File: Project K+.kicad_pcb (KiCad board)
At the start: 2 copper layers, 76.2 x 133.4 mm, 155 parts, among them J1 USB_C_Receptacle_USB2.0, J2 USB Breakout, J3 Conn_01x03_Male, SW1 Rotary_Encoder_Switch, SW2 Rotary_Encoder_Switch, SW3 Rotary_Encoder_Switch, SW4 Rotary_Encoder_Switch, U1 ProMicro, U10 WS2811, U11 WS2811, U12 WS2811, U13 WS2811, U14 WS2811, U15 WS2811, U16 WS2811, U17 WS2811, U18 WS2811, U19 WS2811, U2 WS2811, U20 WS2811, U21 WS2811, U3 WS2811, U4 WS2811, U5 WS2811, U6 WS2811, U7 WS2811, U8 WS2811, U9 WS2811

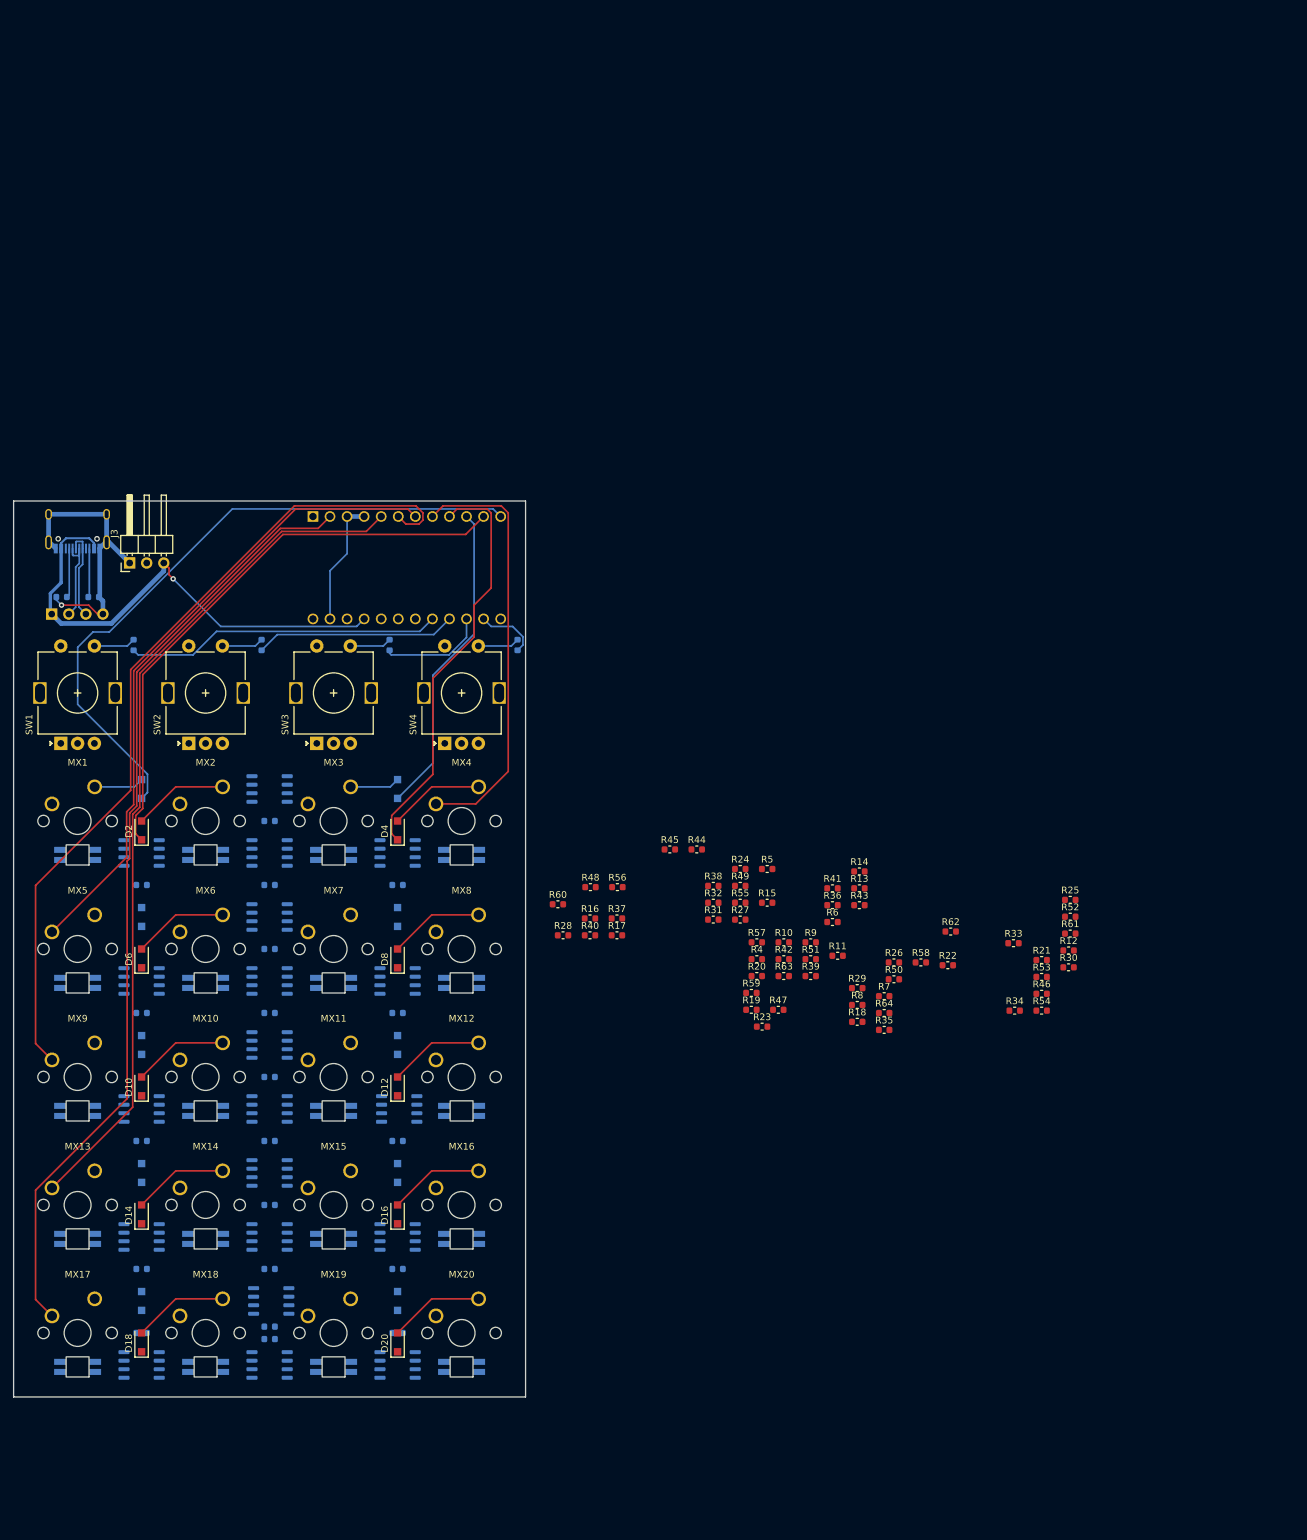
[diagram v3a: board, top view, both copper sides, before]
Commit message: Add 3D keyboard layout
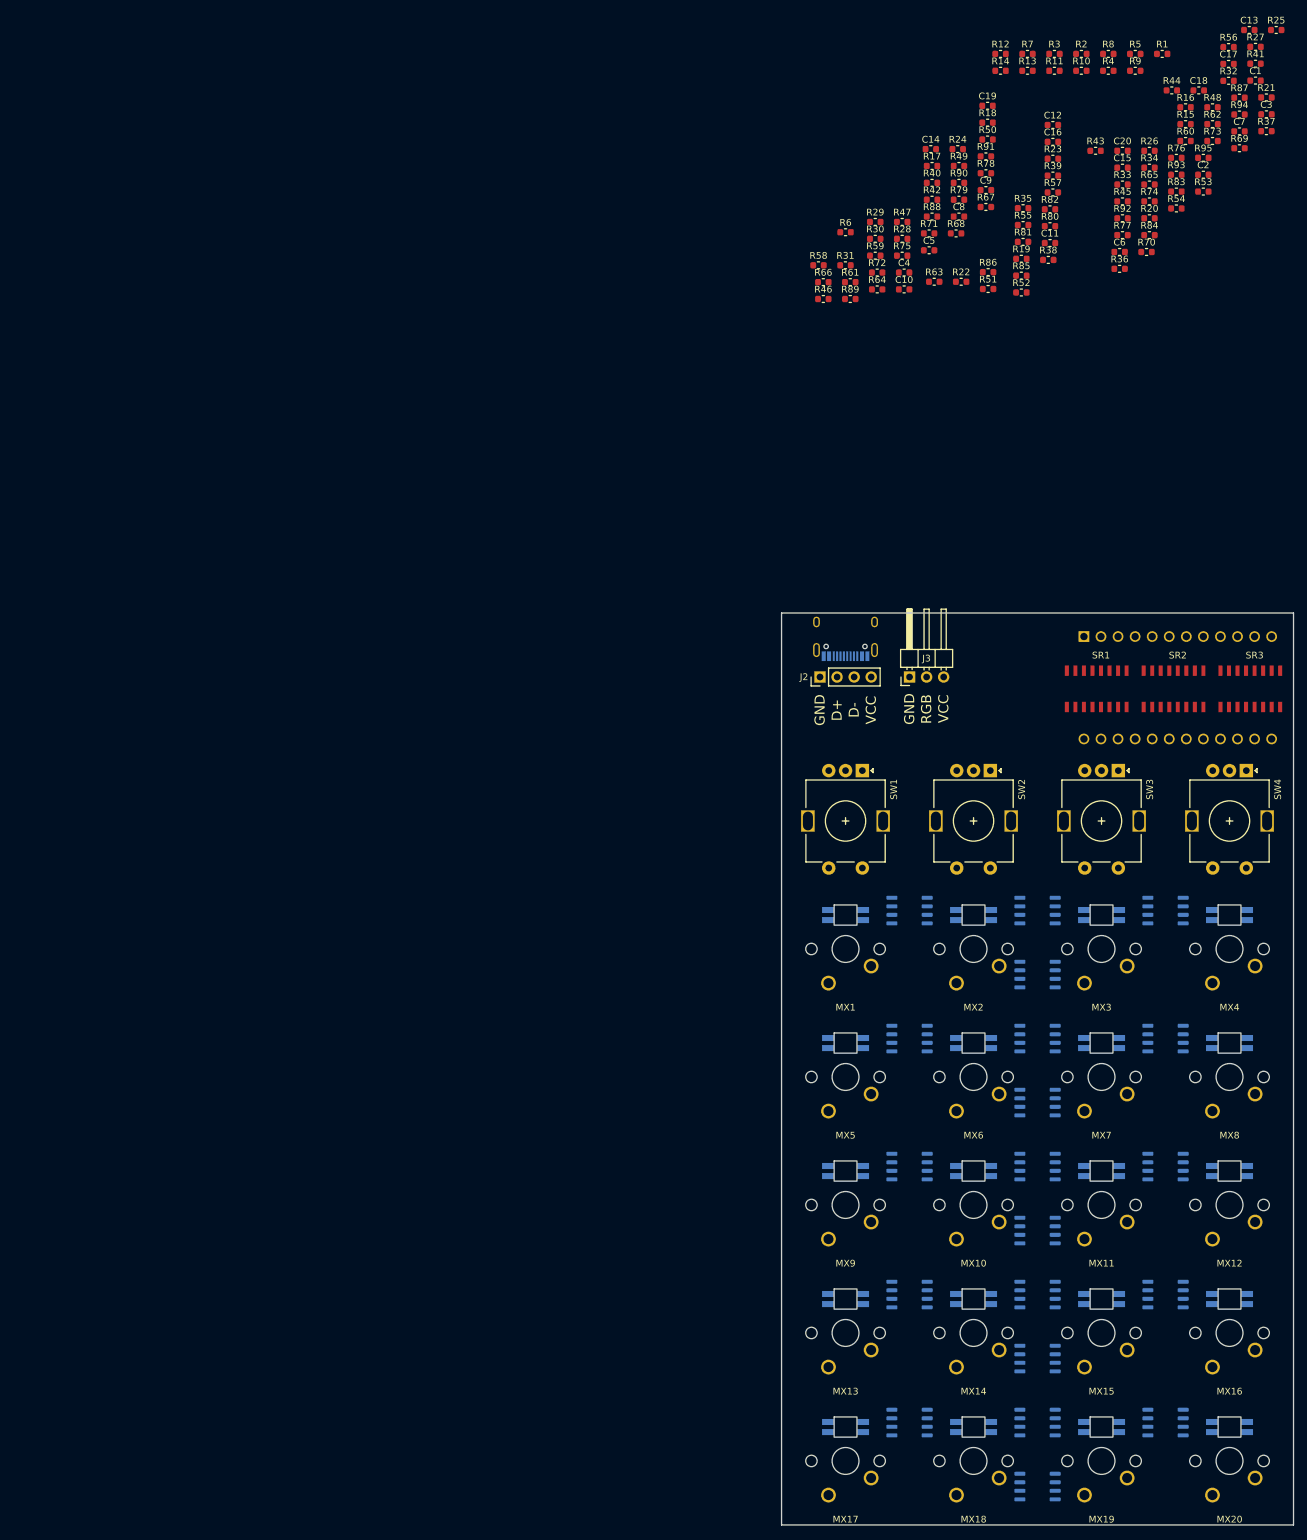
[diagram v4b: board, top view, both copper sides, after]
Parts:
- removed D1, D10, D11, D12, D13, D14, D15, D16, D17, D18, D19, D2, D20, D3, D4, D5, D6, D7, D8, D9: D_ALT, Diode_SMD:D_SOD-123F
- removed U21: WS2811, Package_SO:SOP-8_3.9x4.9mm_P1.27mm
- added ARD1: ProMicro, Arduino_Pro_Micro:ProMicro, B.Cu at (259.0, 56.4)
- added R68: 100R, Resistor_SMD:R_0603_1608Metric, F.Cu at (226.0, -11.2)
- added R69: 100R, Resistor_SMD:R_0603_1608Metric, F.Cu at (268.2, -23.9)
- added R70: 100R, Resistor_SMD:R_0603_1608Metric, F.Cu at (254.3, -8.49)
- added R71: 33R, Resistor_SMD:R_0603_1608Metric, F.Cu at (222.0, -11.2)
- added R72: 33R, Resistor_SMD:R_0603_1608Metric, F.Cu at (214.3, -5.43)
- added R73: 33R, Resistor_SMD:R_0603_1608Metric, F.Cu at (264.2, -25.0)
- added R74: 33R, Resistor_SMD:R_0603_1608Metric, F.Cu at (254.8, -16.0)
- added R75: 33R, Resistor_SMD:R_0603_1608Metric, F.Cu at (218.0, -7.94)
- added R76: 33R, Resistor_SMD:R_0603_1608Metric, F.Cu at (258.8, -22.5)
- added R77: 33R, Resistor_SMD:R_0603_1608Metric, F.Cu at (250.8, -11.0)
- added R78: 33R, Resistor_SMD:R_0603_1608Metric, F.Cu at (230.4, -20.2)
- added R79: 100R, Resistor_SMD:R_0603_1608Metric, F.Cu at (226.4, -16.3)
- added R80: 100R, Resistor_SMD:R_0603_1608Metric, F.Cu at (240.0, -12.3)
- added R81: 100R, Resistor_SMD:R_0603_1608Metric, F.Cu at (236.0, -9.99)
- added R82: 100R, Resistor_SMD:R_0603_1608Metric, F.Cu at (240.0, -14.8)
- added R83: 100R, Resistor_SMD:R_0603_1608Metric, F.Cu at (258.8, -17.5)
- added R84: 100R, Resistor_SMD:R_0603_1608Metric, F.Cu at (254.8, -11.0)
- added R85: 100R, Resistor_SMD:R_0603_1608Metric, F.Cu at (235.7, -4.97)
- added R86: 100R, Resistor_SMD:R_0603_1608Metric, F.Cu at (230.8, -5.49)
- added R87: 33R, Resistor_SMD:R_0603_1608Metric, F.Cu at (268.2, -31.5)
- added R88: 33R, Resistor_SMD:R_0603_1608Metric, F.Cu at (222.4, -13.8)
- added R89: 33R, Resistor_SMD:R_0603_1608Metric, F.Cu at (210.2, -1.49)
- added R90: 33R, Resistor_SMD:R_0603_1608Metric, F.Cu at (226.4, -18.8)
- added R91: 33R, Resistor_SMD:R_0603_1608Metric, F.Cu at (230.4, -22.7)
- added R92: 33R, Resistor_SMD:R_0603_1608Metric, F.Cu at (250.8, -13.5)
- added R93: 33R, Resistor_SMD:R_0603_1608Metric, F.Cu at (258.8, -20.0)
- added R94: 33R, Resistor_SMD:R_0603_1608Metric, F.Cu at (268.2, -28.9)
- added R95: 33R, Resistor_SMD:R_0603_1608Metric, F.Cu at (262.8, -22.5)
- added SR1: 74HC165, Arduino_Pro_Micro:R-PDSO-G16, F.Cu at (242.5, 53.8)
- added SR2: 74HC165, Arduino_Pro_Micro:R-PDSO-G16, F.Cu at (253.9, 53.8)
- added SR3: 74HC165, Arduino_Pro_Micro:R-PDSO-G16, F.Cu at (265.4, 53.8)
- C1, C10, C11, C12, C13, C14, C15, C16, C17, C18, C19, C2, C20, C3, C4, C5, C6, C7, C8, C9, J2, R2: moved to F.Cu
- R1: value 5.1K -> 220R; moved to F.Cu
- R10, R11, R13, R14, R8: value 33R -> 5.1K
- R12, R9: value 33R -> 220R
- R15, R20, R21, R22, R32, R33, R34, R35, R36, R37, R38, R47, R48, R49, R50, R51, R63, R64: value 33R -> 100R
- R28, R29, R30, R40, R41, R42, R43, R55: value 100R -> 33R
- R3: value 220R -> 5.1K; moved to F.Cu
- R4, R5, R7: value 100R -> 5.1K
- R6: value 100R -> 220R
- R65, R66, R67: value 220R -> 100R; moved to F.Cu
- SW1, SW2, SW3, SW4: value Rotary_Encoder_Switch -> (none)
- U1: value ProMicro -> WS2811; footprint Arduino_Pro_Micro:ProMicro -> Package_SO:SOP-8_3.9x4.9mm_P1.27mm
- moved C17 248.7 mm to (266.6, -36.5)
- moved C13 247.4 mm to (269.6, -41.5)
- moved C18 230.2 mm to (262.1, -32.5)
- moved C19 212.4 mm to (230.7, -30.2)
- moved C15 207.3 mm to (250.8, -21.0)
- moved C20 206.4 mm to (250.8, -23.6)
- moved C1 204.5 mm to (270.6, -34.0)
- moved C7 195.1 mm to (268.2, -26.4)
- moved C16 194.0 mm to (240.4, -24.9)
- moved C9 189.3 mm to (230.4, -17.7)
- moved C3 187.5 mm to (272.2, -29.0)
- moved C14 185.4 mm to (222.2, -23.8)
- moved R1 182.7 mm to (256.7, -38.0)
- moved C12 179.9 mm to (240.4, -27.4)
- moved C11 177.1 mm to (240.0, -9.82)
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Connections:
- J2 pad 1: +5V -> GND
- J2 pad 2: D- -> D+
- J2 pad 3: D+ -> D-
- J2 pad 4: GND -> +5V
- MX1 pad 5: Row0 -> GND
- MX1 pad 6: Net-(D1-Pad2) -> Net-(MX1-Pad6)
- MX10 pad 5: Row2 -> GND
- MX10 pad 6: Net-(D10-Pad2) -> Net-(MX10-Pad6)
- MX11 pad 5: Row2 -> GND
- MX11 pad 6: Net-(D11-Pad2) -> Net-(MX11-Pad6)
- MX12 pad 5: Row2 -> GND
- MX12 pad 6: Net-(D12-Pad2) -> Net-(MX12-Pad6)
- MX13 pad 5: Row3 -> GND
- MX13 pad 6: Net-(D13-Pad2) -> Net-(MX13-Pad6)
- MX14 pad 5: Row3 -> GND
- MX15 pad 5: Row3 -> GND
- MX16 pad 5: Row3 -> GND
- MX17 pad 5: Row4 -> GND
- MX18 pad 5: Row4 -> GND
- MX19 pad 5: Row4 -> GND
- MX2 pad 5: Row0 -> GND
- MX2 pad 6: Net-(D2-Pad2) -> Net-(MX2-Pad6)
- MX20 pad 5: Row4 -> GND
- MX3 pad 5: Row0 -> GND
- MX3 pad 6: Net-(D3-Pad2) -> Net-(MX3-Pad6)
- MX4 pad 5: Row0 -> GND
- MX4 pad 6: Net-(D4-Pad2) -> Net-(MX4-Pad6)
- MX5 pad 5: Row1 -> GND
- MX5 pad 6: Net-(D5-Pad2) -> Net-(MX5-Pad6)
- MX6 pad 5: Row1 -> GND
- MX6 pad 6: Net-(D6-Pad2) -> Net-(MX6-Pad6)
- MX7 pad 5: Row1 -> GND
- MX7 pad 6: Net-(D7-Pad2) -> Net-(MX7-Pad6)
- MX8 pad 5: Row1 -> GND
- MX8 pad 6: Net-(D8-Pad2) -> Net-(MX8-Pad6)
- MX9 pad 5: Row2 -> GND
- MX9 pad 6: Net-(D9-Pad2) -> Net-(MX9-Pad6)
- R1 pad 1: GND -> SW4
- R1 pad 2: Net-(J1-PadA5) -> Net-(R1-Pad2)
- R10 pad 1: Net-(R10-Pad1) -> A3
- R10 pad 2: Net-(R10-Pad2) -> +5V
- R11 pad 1: Net-(R11-Pad1) -> +5V
- R11 pad 2: Net-(R11-Pad2) -> B3
- R12 pad 1: Net-(R12-Pad1) -> SW1
- R13 pad 1: Net-(R13-Pad1) -> A4
- R13 pad 2: Net-(R10-Pad2) -> +5V
- R14 pad 1: Net-(R14-Pad1) -> +5V
- R14 pad 2: Net-(R11-Pad2) -> B4
- R15 pad 1: Net-(R15-Pad1) -> +5V
- R15 pad 2: Net-(R15-Pad2) -> Net-(C1-Pad2)
- R16 pad 2: Net-(C5-Pad2) -> Net-(C2-Pad2)
- R17 pad 2: Net-(C6-Pad2) -> Net-(C3-Pad2)
- R18 pad 2: Net-(C7-Pad2) -> Net-(C4-Pad2)
- R19 pad 1: +5V -> Net-(R19-Pad1)
- R19 pad 2: Net-(C8-Pad2) -> Net-(MX1-Pad6)
- R2 pad 1: Net-(J1-PadB5) -> GND
- R2 pad 2: GND -> Net-(J1-PadA5)
- R20 pad 2: Net-(R20-Pad2) -> Net-(MX2-Pad6)
- R21 pad 2: Net-(R21-Pad2) -> Net-(MX3-Pad6)
- R22 pad 2: Net-(R22-Pad2) -> Net-(MX4-Pad6)
- R23 pad 2: Net-(R15-Pad2) -> RGB
- R25 pad 2: Net-(R20-Pad2) -> Net-(R25-Pad2)
- R26 pad 2: Net-(R21-Pad2) -> Net-(R26-Pad2)
- R27 pad 2: Net-(R22-Pad2) -> Net-(R24-Pad2)
- R28 pad 1: +5V -> Net-(R28-Pad1)
- R28 pad 2: Net-(C9-Pad2) -> Net-(R25-Pad2)
- R29 pad 1: +5V -> Net-(R29-Pad1)
- R29 pad 2: Net-(C10-Pad2) -> Net-(R26-Pad2)
- R3 pad 1: SW1 -> Net-(J1-PadB5)
- R3 pad 2: Net-(R3-Pad2) -> GND
- R30 pad 1: +5V -> Net-(R30-Pad1)
- R30 pad 2: Net-(C11-Pad2) -> Net-(R30-Pad2)
- R31 pad 2: Net-(C12-Pad2) -> Net-(C5-Pad2)
- R32 pad 1: Net-(R32-Pad1) -> +5V
- R32 pad 2: Net-(R24-Pad2) -> Net-(C6-Pad2)
- R33 pad 1: Net-(R33-Pad1) -> +5V
- R33 pad 2: Net-(R33-Pad2) -> Net-(C7-Pad2)
- R34 pad 1: Net-(R34-Pad1) -> +5V
- R34 pad 2: Net-(R34-Pad2) -> Net-(C8-Pad2)
- R35 pad 2: Net-(R35-Pad2) -> Net-(MX5-Pad6)
- R36 pad 2: Net-(R33-Pad2) -> Net-(MX6-Pad6)
- R37 pad 2: Net-(R34-Pad2) -> Net-(MX7-Pad6)
- R38 pad 2: Net-(R35-Pad2) -> Net-(MX8-Pad6)
- R4 pad 1: +5V -> A1
- R4 pad 2: Net-(C1-Pad2) -> +5V
- R40 pad 1: +5V -> Net-(R40-Pad1)
- R40 pad 2: Net-(C13-Pad2) -> Net-(R40-Pad2)
- R41 pad 1: +5V -> Net-(R41-Pad1)
- R41 pad 2: Net-(C14-Pad2) -> Net-(R41-Pad2)
- R42 pad 1: +5V -> Net-(R42-Pad1)
- R42 pad 2: Net-(C15-Pad2) -> Net-(R30-Pad2)
- R43 pad 1: +5V -> Net-(R43-Pad1)
- R43 pad 2: Net-(C16-Pad2) -> Net-(R43-Pad2)
- R44 pad 2: Net-(R44-Pad2) -> Net-(R39-Pad2)
- R45 pad 2: Net-(R45-Pad2) -> Net-(R40-Pad2)
- R46 pad 2: Net-(R46-Pad2) -> Net-(R41-Pad2)
- R47 pad 1: Net-(R47-Pad1) -> +5V
- R47 pad 2: Net-(R39-Pad2) -> Net-(C9-Pad2)
- R48 pad 1: Net-(R48-Pad1) -> +5V
- R48 pad 2: Net-(R48-Pad2) -> Net-(C10-Pad2)
- R49 pad 1: Net-(R49-Pad1) -> +5V
- R49 pad 2: Net-(R44-Pad2) -> Net-(C11-Pad2)
- R5 pad 2: Net-(C2-Pad2) -> B1
- R50 pad 1: Net-(R50-Pad1) -> +5V
- R50 pad 2: Net-(R45-Pad2) -> Net-(C12-Pad2)
- R51 pad 2: Net-(R46-Pad2) -> Net-(MX9-Pad6)
- R52 pad 1: +5V -> Net-(R52-Pad1)
- R52 pad 2: Net-(C17-Pad2) -> Net-(MX10-Pad6)
- R53 pad 1: +5V -> Net-(R53-Pad1)
- R53 pad 2: Net-(C18-Pad2) -> Net-(MX11-Pad6)
- R54 pad 1: +5V -> Net-(R54-Pad1)
- R54 pad 2: Net-(C19-Pad2) -> Net-(MX12-Pad6)
- R55 pad 1: +5V -> Net-(R55-Pad1)
- R55 pad 2: Net-(C20-Pad2) -> Net-(R43-Pad2)
- R56 pad 2: Net-(R48-Pad2) -> Net-(R56-Pad2)
- R59 pad 2: Net-(R59-Pad2) -> Net-(R56-Pad2)
- R6 pad 1: +5V -> SW3
- R6 pad 2: Net-(C3-Pad2) -> Net-(R6-Pad2)
- R62 pad 2: Net-(R59-Pad2) -> Net-(R62-Pad2)
- R63 pad 1: Net-(R63-Pad1) -> +5V
- R63 pad 2: Net-(R63-Pad2) -> Net-(C13-Pad2)
- R64 pad 1: Net-(J3-Pad2) -> +5V
- R64 pad 2: Net-(R63-Pad1) -> Net-(C14-Pad2)
- R65 pad 1: SW4 -> +5V
- R65 pad 2: Net-(R65-Pad2) -> Net-(C15-Pad2)
- R66 pad 1: SW3 -> +5V
- R66 pad 2: Net-(R66-Pad2) -> Net-(C16-Pad2)
- R67 pad 1: SW2 -> Net-(R67-Pad1)
- R67 pad 2: Net-(R67-Pad2) -> Net-(MX13-Pad6)
- R7 pad 1: +5V -> A2
- R7 pad 2: Net-(C4-Pad2) -> +5V
- R8 pad 1: Net-(R8-Pad1) -> +5V
- R8 pad 2: RGB -> B2
- R9 pad 1: Net-(R9-Pad1) -> SW2
- R9 pad 2: Net-(R12-Pad2) -> Net-(R9-Pad2)
- SW1 pad A: Net-(SW1-PadA) -> A1
- SW1 pad B: Net-(SW1-PadB) -> B1
- SW1 pad C: Net-(SW1-PadC) -> GND
- SW1 pad S1: Net-(R65-Pad2) -> Net-(R1-Pad2)
- SW2 pad A: Net-(SW2-PadA) -> A2
- SW2 pad B: Net-(SW2-PadB) -> B2
- SW2 pad C: Net-(SW2-PadC) -> GND
- SW2 pad S1: Net-(R66-Pad2) -> Net-(R6-Pad2)
- SW3 pad A: Net-(SW3-PadA) -> A3
- SW3 pad B: Net-(SW3-PadB) -> B3
- SW3 pad C: Net-(SW3-PadC) -> GND
- SW3 pad S1: Net-(R67-Pad2) -> Net-(R9-Pad2)
- SW4 pad A: Net-(SW4-PadA) -> A4
- SW4 pad B: Net-(SW4-PadB) -> B4
- SW4 pad C: Net-(SW4-PadC) -> GND
- SW4 pad S1: Net-(R3-Pad2) -> Net-(R12-Pad2)
- U1 pad 1: Net-(U1-Pad1) -> Net-(MX1-Pad2)
- U1 pad 2: Row4 -> Net-(MX1-Pad4)
- U1 pad 3: GND -> Net-(MX1-Pad1)
- U1 pad 5: Row3 -> Net-(R27-Pad1)
- U1 pad 6: Row2 -> Net-(R23-Pad1)
- U1 pad 7: Row1 -> Net-(U1-Pad7)
- U1 pad 8: Row0 -> Net-(C1-Pad2)
- U10 pad 1: Net-(MX9-Pad2) -> Net-(MX10-Pad2)
- U10 pad 2: Net-(MX9-Pad4) -> Net-(MX10-Pad4)
- U10 pad 3: Net-(MX9-Pad1) -> Net-(MX10-Pad1)
- U10 pad 5: Net-(R36-Pad1) -> Net-(R60-Pad1)
- U10 pad 6: Net-(R32-Pad1) -> Net-(R56-Pad1)
- U10 pad 8: Net-(C9-Pad2) -> Net-(C10-Pad2)
- U11 pad 1: Net-(MX10-Pad2) -> Net-(MX11-Pad2)
- U11 pad 2: Net-(MX10-Pad4) -> Net-(MX11-Pad4)
- U11 pad 3: Net-(MX10-Pad1) -> Net-(MX11-Pad1)
- U11 pad 5: Net-(R37-Pad1) -> Net-(R61-Pad1)
- U11 pad 6: Net-(R33-Pad1) -> Net-(R57-Pad1)
- U11 pad 8: Net-(C10-Pad2) -> Net-(C11-Pad2)
- U12 pad 1: Net-(MX11-Pad2) -> Net-(MX12-Pad2)
- U12 pad 2: Net-(MX11-Pad4) -> Net-(MX12-Pad4)
- U12 pad 3: Net-(MX11-Pad1) -> Net-(MX12-Pad1)
- U12 pad 5: Net-(R38-Pad1) -> Net-(R62-Pad1)
- U12 pad 6: Net-(R34-Pad1) -> Net-(R58-Pad1)
- U12 pad 8: Net-(C11-Pad2) -> Net-(C12-Pad2)
- U13 pad 1: Net-(MX12-Pad2) -> Net-(MX13-Pad2)
- U13 pad 2: Net-(MX12-Pad4) -> Net-(MX13-Pad4)
- U13 pad 3: Net-(MX12-Pad1) -> Net-(MX13-Pad1)
- U13 pad 5: Net-(R39-Pad1) -> Net-(R75-Pad1)
- U13 pad 6: Net-(R35-Pad1) -> Net-(R71-Pad1)
- U13 pad 8: Net-(C12-Pad2) -> Net-(C13-Pad2)
- U14 pad 1: Net-(MX13-Pad2) -> Net-(MX14-Pad2)
- U14 pad 2: Net-(MX13-Pad4) -> Net-(MX14-Pad4)
- U14 pad 3: Net-(MX13-Pad1) -> Net-(MX14-Pad1)
- U14 pad 5: Net-(R48-Pad1) -> Net-(R76-Pad1)
- U14 pad 6: Net-(R44-Pad1) -> Net-(R72-Pad1)
- U14 pad 8: Net-(C13-Pad2) -> Net-(C14-Pad2)
- U15 pad 1: Net-(MX14-Pad2) -> Net-(MX15-Pad2)
- U15 pad 2: Net-(MX14-Pad4) -> Net-(MX15-Pad4)
- U15 pad 3: Net-(MX14-Pad1) -> Net-(MX15-Pad1)
- U15 pad 5: Net-(R49-Pad1) -> Net-(R77-Pad1)
- U15 pad 6: Net-(R45-Pad1) -> Net-(R73-Pad1)
- U15 pad 8: Net-(C14-Pad2) -> Net-(C15-Pad2)
- U16 pad 1: Net-(MX15-Pad2) -> Net-(MX16-Pad2)
- U16 pad 2: Net-(MX15-Pad4) -> Net-(MX16-Pad4)
- U16 pad 3: Net-(MX15-Pad1) -> Net-(MX16-Pad1)
- U16 pad 5: Net-(R50-Pad1) -> Net-(R78-Pad1)
- U16 pad 6: Net-(R46-Pad1) -> Net-(R74-Pad1)
- U16 pad 8: Net-(C15-Pad2) -> Net-(C16-Pad2)
- U17 pad 1: Net-(MX16-Pad2) -> Net-(MX17-Pad2)
- U17 pad 2: Net-(MX16-Pad4) -> Net-(MX17-Pad4)
- U17 pad 3: Net-(MX16-Pad1) -> Net-(MX17-Pad1)
- U17 pad 5: Net-(R51-Pad1) -> Net-(R91-Pad1)
- U17 pad 6: Net-(R47-Pad1) -> Net-(R87-Pad1)
- U17 pad 8: Net-(C16-Pad2) -> Net-(C17-Pad2)
- U18 pad 1: Net-(MX17-Pad2) -> Net-(MX18-Pad2)
- U18 pad 2: Net-(MX17-Pad4) -> Net-(MX18-Pad4)
- U18 pad 3: Net-(MX17-Pad1) -> Net-(MX18-Pad1)
- U18 pad 5: Net-(R60-Pad1) -> Net-(R92-Pad1)
- U18 pad 6: Net-(R56-Pad1) -> Net-(R88-Pad1)
- U18 pad 8: Net-(C17-Pad2) -> Net-(C18-Pad2)
- U19 pad 1: Net-(MX18-Pad2) -> Net-(MX19-Pad2)
- U19 pad 2: Net-(MX18-Pad4) -> Net-(MX19-Pad4)
- U19 pad 3: Net-(MX18-Pad1) -> Net-(MX19-Pad1)
- U19 pad 5: Net-(R61-Pad1) -> Net-(R93-Pad1)
- U19 pad 6: Net-(R57-Pad1) -> Net-(R89-Pad1)
- U19 pad 8: Net-(C18-Pad2) -> Net-(C19-Pad2)
- U2 pad 1: Net-(MX1-Pad2) -> Net-(MX2-Pad2)
- U2 pad 2: Net-(MX1-Pad4) -> Net-(MX2-Pad4)
- U2 pad 3: Net-(MX1-Pad1) -> Net-(MX2-Pad1)
- U2 pad 5: Net-(R12-Pad1) -> Net-(R28-Pad1)
- U2 pad 6: Net-(R8-Pad1) -> Net-(R24-Pad1)
- U2 pad 8: Net-(C1-Pad2) -> Net-(C2-Pad2)
- U20 pad 1: Net-(MX19-Pad2) -> Net-(MX20-Pad2)
- U20 pad 2: Net-(MX19-Pad4) -> Net-(MX20-Pad4)
- U20 pad 3: Net-(MX19-Pad1) -> Net-(MX20-Pad1)
- U20 pad 5: Net-(R62-Pad1) -> Net-(R94-Pad2)
- U20 pad 6: Net-(R58-Pad1) -> Net-(R90-Pad1)
- U20 pad 8: Net-(C19-Pad2) -> Net-(C20-Pad2)
- U3 pad 1: Net-(MX2-Pad2) -> Net-(MX3-Pad2)
- U3 pad 2: Net-(MX2-Pad4) -> Net-(MX3-Pad4)
- U3 pad 3: Net-(MX2-Pad1) -> Net-(MX3-Pad1)
- U3 pad 5: Net-(R13-Pad1) -> Net-(R29-Pad1)
- U3 pad 6: Net-(R9-Pad1) -> Net-(R25-Pad1)
- U3 pad 8: Net-(C2-Pad2) -> Net-(C3-Pad2)
- U4 pad 1: Net-(MX3-Pad2) -> Net-(MX4-Pad2)
- U4 pad 2: Net-(MX3-Pad4) -> Net-(MX4-Pad4)
- U4 pad 3: Net-(MX3-Pad1) -> Net-(MX4-Pad1)
- U4 pad 5: Net-(R14-Pad1) -> Net-(R30-Pad1)
- U4 pad 6: Net-(R10-Pad1) -> Net-(R26-Pad1)
- U4 pad 8: Net-(C3-Pad2) -> Net-(C4-Pad2)
- U5 pad 1: Net-(MX4-Pad2) -> Net-(MX5-Pad2)
- U5 pad 2: Net-(MX4-Pad4) -> Net-(MX5-Pad4)
- U5 pad 3: Net-(MX4-Pad1) -> Net-(MX5-Pad1)
- U5 pad 5: Net-(R15-Pad1) -> Net-(R43-Pad1)
- U5 pad 6: Net-(R11-Pad1) -> Net-(R39-Pad1)
- U5 pad 8: Net-(C4-Pad2) -> Net-(C5-Pad2)
- U6 pad 1: Net-(MX5-Pad2) -> Net-(MX6-Pad2)
- U6 pad 2: Net-(MX5-Pad4) -> Net-(MX6-Pad4)
- U6 pad 3: Net-(MX5-Pad1) -> Net-(MX6-Pad1)
- U6 pad 5: Net-(R24-Pad1) -> Net-(R44-Pad1)
- U6 pad 6: Net-(R20-Pad1) -> Net-(R40-Pad1)
- U6 pad 8: Net-(C5-Pad2) -> Net-(C6-Pad2)
- U7 pad 1: Net-(MX6-Pad2) -> Net-(MX7-Pad2)
- U7 pad 2: Net-(MX6-Pad4) -> Net-(MX7-Pad4)
- U7 pad 3: Net-(MX6-Pad1) -> Net-(MX7-Pad1)
- U7 pad 5: Net-(R25-Pad1) -> Net-(R45-Pad1)
- U7 pad 6: Net-(R21-Pad1) -> Net-(R41-Pad1)
- U7 pad 8: Net-(C6-Pad2) -> Net-(C7-Pad2)
- U8 pad 1: Net-(MX7-Pad2) -> Net-(MX8-Pad2)
- U8 pad 2: Net-(MX7-Pad4) -> Net-(MX8-Pad4)
- U8 pad 3: Net-(MX7-Pad1) -> Net-(MX8-Pad1)
- U8 pad 5: Net-(R26-Pad1) -> Net-(R46-Pad1)
- U8 pad 6: Net-(R22-Pad1) -> Net-(R42-Pad1)
- U8 pad 8: Net-(C7-Pad2) -> Net-(C8-Pad2)
- U9 pad 1: Net-(MX8-Pad2) -> Net-(MX9-Pad2)
- U9 pad 2: Net-(MX8-Pad4) -> Net-(MX9-Pad4)
- U9 pad 3: Net-(MX8-Pad1) -> Net-(MX9-Pad1)
- U9 pad 5: Net-(R27-Pad1) -> Net-(R59-Pad1)
- U9 pad 6: Net-(R23-Pad1) -> Net-(R55-Pad1)
- U9 pad 8: Net-(C8-Pad2) -> Net-(C9-Pad2)
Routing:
- net Row4: track 141.4 -> 0.00 mm
- net Row3: track 127.6 -> 0.00 mm
- net Row2: track 124.4 -> 0.00 mm
- net Col0: track 99.1 -> 0.00 mm
- net Row1: track 96.3 -> 0.00 mm
- net Col1: track 85.9 -> 0.00 mm
- net +5V: track 74.1 -> 0.00 mm, vias 1 -> 0
- net Row0: track 63.6 -> 0.00 mm
- net Col3: track 62.1 -> 0.00 mm
- net GND: track 61.6 -> 0.00 mm, vias 1 -> 0
- net Col2: track 47.1 -> 0.00 mm
- net SW4: track 47.0 -> 0.00 mm
- net SW3: track 29.9 -> 0.00 mm
- net SW2: track 15.8 -> 0.00 mm
- net Net-(MX18-Pad6): track 14.2 -> 0.00 mm
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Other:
- board size 76.2 x 133.4 mm -> 76.2 x 135.7 mm
- board text added: "D+"
- board text added: "D-"
- board text added: "GND"
- board text added: "RGB"
- board text added: "VCC"

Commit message: Update PCB
Added switch and LED layout
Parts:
- removed C1, C10, C11, C12, C13, C14, C15, C16, C17, C18, C19, C2, C20, C3, C4, C5, C6, C7, C8, C9: 100n, Capacitor_SMD:C_0603_1608Metric
- removed J3: Conn_01x03_Male, Connector_PinHeader_2.54mm:PinHeader_1x03_P2.54mm_Horizontal
- removed MX1, MX10, MX11, MX12, MX13, MX14, MX15, MX16, MX17, MX18, MX19, MX2, MX20, MX3, MX4, MX5, MX6, MX7, MX8, MX9: Cherry_MX_RGB, Cherry_MX_SMD:Cherry-MX_PCB-Mounted_LTST-A683CEGBW_Mill-Max-7305
- removed R24, R25, R26, R27, R28, R29, R30, R39, R40, R41, R42, R43, R44, R45, R46, R55, R56, R57, R58, R59, R60, R61, R62, R71, R72, R73, R74, R75, R76, R77, R78, R87, R88, R89, R90, R91, R92, R93, R94, R95: 33R, Resistor_SMD:R_0603_1608Metric
- removed R31, R32, R33, R34, R35, R36, R37, R38, R47, R48, R49, R50, R51, R52, R53, R54, R63, R64, R65, R66, R67, R68, R69, R70, R79, R80, R81, R82, R83, R84, R85, R86: 100R, Resistor_SMD:R_0603_1608Metric
- removed SW1, SW2, SW3, SW4: , Rotary_Encoder:RotaryEncoder_Alps_EC11E-Switch_Vertical_H20mm
- removed U1, U10, U11, U12, U13, U14, U15, U16, U17, U18, U19, U2, U20, U3, U4, U5, U6, U7, U8, U9: WS2811, Package_SO:SOP-8_3.9x4.9mm_P1.27mm
- added RE1: , Rotary_Encoder:RotaryEncoder_Alps_EC11E-Switch_Vertical_H20mm, F.Cu at (317.0, 123.2)
- added RE2: , Rotary_Encoder:RotaryEncoder_Alps_EC11E-Switch_Vertical_H20mm, F.Cu at (336.1, 123.2)
- added RE3: , Rotary_Encoder:RotaryEncoder_Alps_EC11E-Switch_Vertical_H20mm, F.Cu at (355.1, 123.2)
- added RE4: , Rotary_Encoder:RotaryEncoder_Alps_EC11E-Switch_Vertical_H20mm, F.Cu at (393.2, 123.2)
- added RE5: , Rotary_Encoder:RotaryEncoder_Alps_EC11E-Switch_Vertical_H20mm, F.Cu at (412.3, 123.2)
- added RE6: , Rotary_Encoder:RotaryEncoder_Alps_EC11E-Switch_Vertical_H20mm, F.Cu at (431.3, 123.2)
- added RE7: , Rotary_Encoder:RotaryEncoder_Alps_EC11E-Switch_Vertical_H20mm, F.Cu at (450.4, 123.2)
- added RGB1: WS2812B, LED_SMD:LED_WS2812B_PLCC4_5.0x5.0mm_P3.2mm, F.Cu at (-6.83, 117.2)
- added RGB10: WS2812B, LED_SMD:LED_WS2812B_PLCC4_5.0x5.0mm_P3.2mm, F.Cu at (31.3, 136.3)
- added RGB100: WS2812B, LED_SMD:LED_WS2812B_PLCC4_5.0x5.0mm_P3.2mm, F.Cu at (450.4, 174.4)
- added RGB101: WS2812B, LED_SMD:LED_WS2812B_PLCC4_5.0x5.0mm_P3.2mm, F.Cu at (393.2, 193.4)
- added RGB102: WS2812B, LED_SMD:LED_WS2812B_PLCC4_5.0x5.0mm_P3.2mm, F.Cu at (412.3, 193.4)
- added RGB103: WS2812B, LED_SMD:LED_WS2812B_PLCC4_5.0x5.0mm_P3.2mm, F.Cu at (431.3, 193.4)
- added RGB104: WS2812B, LED_SMD:LED_WS2812B_PLCC4_5.0x5.0mm_P3.2mm, F.Cu at (450.4, 193.4)
- added RGB105: WS2812B, LED_SMD:LED_WS2812B_PLCC4_5.0x5.0mm_P3.2mm, F.Cu at (393.2, 212.5)
- added RGB106: WS2812B, LED_SMD:LED_WS2812B_PLCC4_5.0x5.0mm_P3.2mm, F.Cu at (412.3, 212.5)
- added RGB107: WS2812B, LED_SMD:LED_WS2812B_PLCC4_5.0x5.0mm_P3.2mm, F.Cu at (431.3, 212.5)
- added RGB108: WS2812B, LED_SMD:LED_WS2812B_PLCC4_5.0x5.0mm_P3.2mm, F.Cu at (450.4, 212.5)
- added RGB11: WS2812B, LED_SMD:LED_WS2812B_PLCC4_5.0x5.0mm_P3.2mm, F.Cu at (50.3, 136.3)
- added RGB12: WS2812B, LED_SMD:LED_WS2812B_PLCC4_5.0x5.0mm_P3.2mm, F.Cu at (69.4, 136.3)
- added RGB13: WS2812B, LED_SMD:LED_WS2812B_PLCC4_5.0x5.0mm_P3.2mm, F.Cu at (88.4, 136.3)
- added RGB14: WS2812B, LED_SMD:LED_WS2812B_PLCC4_5.0x5.0mm_P3.2mm, F.Cu at (107.5, 136.3)
- added RGB15: WS2812B, LED_SMD:LED_WS2812B_PLCC4_5.0x5.0mm_P3.2mm, F.Cu at (-2.06, 155.3)
- added RGB16: WS2812B, LED_SMD:LED_WS2812B_PLCC4_5.0x5.0mm_P3.2mm, F.Cu at (21.7, 155.3)
- added RGB17: WS2812B, LED_SMD:LED_WS2812B_PLCC4_5.0x5.0mm_P3.2mm, F.Cu at (40.9, 155.3)
- added RGB18: WS2812B, LED_SMD:LED_WS2812B_PLCC4_5.0x5.0mm_P3.2mm, F.Cu at (59.8, 155.3)
- added RGB19: WS2812B, LED_SMD:LED_WS2812B_PLCC4_5.0x5.0mm_P3.2mm, F.Cu at (78.9, 155.3)
- added RGB2: WS2812B, LED_SMD:LED_WS2812B_PLCC4_5.0x5.0mm_P3.2mm, F.Cu at (12.2, 117.2)
- added RGB20: WS2812B, LED_SMD:LED_WS2812B_PLCC4_5.0x5.0mm_P3.2mm, F.Cu at (97.9, 155.3)
- added RGB21: WS2812B, LED_SMD:LED_WS2812B_PLCC4_5.0x5.0mm_P3.2mm, F.Cu at (0.32, 174.4)
- added RGB22: WS2812B, LED_SMD:LED_WS2812B_PLCC4_5.0x5.0mm_P3.2mm, F.Cu at (26.5, 174.4)
- added RGB23: WS2812B, LED_SMD:LED_WS2812B_PLCC4_5.0x5.0mm_P3.2mm, F.Cu at (45.6, 174.4)
- added RGB24: WS2812B, LED_SMD:LED_WS2812B_PLCC4_5.0x5.0mm_P3.2mm, F.Cu at (64.6, 174.4)
- added RGB25: WS2812B, LED_SMD:LED_WS2812B_PLCC4_5.0x5.0mm_P3.2mm, F.Cu at (83.7, 174.4)
- added RGB26: WS2812B, LED_SMD:LED_WS2812B_PLCC4_5.0x5.0mm_P3.2mm, F.Cu at (102.7, 174.4)
- added RGB27: WS2812B, LED_SMD:LED_WS2812B_PLCC4_5.0x5.0mm_P3.2mm, F.Cu at (5.08, 193.4)
- added RGB28: WS2812B, LED_SMD:LED_WS2812B_PLCC4_5.0x5.0mm_P3.2mm, F.Cu at (36.0, 193.4)
- added RGB29: WS2812B, LED_SMD:LED_WS2812B_PLCC4_5.0x5.0mm_P3.2mm, F.Cu at (55.1, 193.4)
- added RGB3: WS2812B, LED_SMD:LED_WS2812B_PLCC4_5.0x5.0mm_P3.2mm, F.Cu at (31.3, 117.2)
- added RGB30: WS2812B, LED_SMD:LED_WS2812B_PLCC4_5.0x5.0mm_P3.2mm, F.Cu at (74.1, 193.4)
- added RGB31: WS2812B, LED_SMD:LED_WS2812B_PLCC4_5.0x5.0mm_P3.2mm, F.Cu at (93.2, 193.4)
- added RGB32: WS2812B, LED_SMD:LED_WS2812B_PLCC4_5.0x5.0mm_P3.2mm, F.Cu at (-4.45, 212.5)
- added RGB33: WS2812B, LED_SMD:LED_WS2812B_PLCC4_5.0x5.0mm_P3.2mm, F.Cu at (19.4, 212.5)
- added RGB34: WS2812B, LED_SMD:LED_WS2812B_PLCC4_5.0x5.0mm_P3.2mm, F.Cu at (43.2, 212.5)
- added RGB35: WS2812B, LED_SMD:LED_WS2812B_PLCC4_5.0x5.0mm_P3.2mm, F.Cu at (83.7, 212.5)
- added RGB36: WS2812B, LED_SMD:LED_WS2812B_PLCC4_5.0x5.0mm_P3.2mm, F.Cu at (145.6, 117.2)
- added RGB37: WS2812B, LED_SMD:LED_WS2812B_PLCC4_5.0x5.0mm_P3.2mm, F.Cu at (164.6, 117.2)
- added RGB38: WS2812B, LED_SMD:LED_WS2812B_PLCC4_5.0x5.0mm_P3.2mm, F.Cu at (183.7, 117.2)
- added RGB39: WS2812B, LED_SMD:LED_WS2812B_PLCC4_5.0x5.0mm_P3.2mm, F.Cu at (202.7, 117.2)
- added RGB4: WS2812B, LED_SMD:LED_WS2812B_PLCC4_5.0x5.0mm_P3.2mm, F.Cu at (50.3, 117.2)
- added RGB40: WS2812B, LED_SMD:LED_WS2812B_PLCC4_5.0x5.0mm_P3.2mm, F.Cu at (221.8, 117.2)
- added RGB41: WS2812B, LED_SMD:LED_WS2812B_PLCC4_5.0x5.0mm_P3.2mm, F.Cu at (240.8, 117.2)
- added RGB42: WS2812B, LED_SMD:LED_WS2812B_PLCC4_5.0x5.0mm_P3.2mm, F.Cu at (145.6, 136.3)
- added RGB43: WS2812B, LED_SMD:LED_WS2812B_PLCC4_5.0x5.0mm_P3.2mm, F.Cu at (164.6, 136.3)
- added RGB44: WS2812B, LED_SMD:LED_WS2812B_PLCC4_5.0x5.0mm_P3.2mm, F.Cu at (183.6, 136.3)
- added RGB45: WS2812B, LED_SMD:LED_WS2812B_PLCC4_5.0x5.0mm_P3.2mm, F.Cu at (202.7, 136.3)
- added RGB46: WS2812B, LED_SMD:LED_WS2812B_PLCC4_5.0x5.0mm_P3.2mm, F.Cu at (221.8, 136.3)
- added RGB47: WS2812B, LED_SMD:LED_WS2812B_PLCC4_5.0x5.0mm_P3.2mm, F.Cu at (240.8, 136.3)
- added RGB48: WS2812B, LED_SMD:LED_WS2812B_PLCC4_5.0x5.0mm_P3.2mm, F.Cu at (269.4, 136.3)
- added RGB49: WS2812B, LED_SMD:LED_WS2812B_PLCC4_5.0x5.0mm_P3.2mm, F.Cu at (136.0, 155.3)
- added RGB5: WS2812B, LED_SMD:LED_WS2812B_PLCC4_5.0x5.0mm_P3.2mm, F.Cu at (69.4, 117.2)
- added RGB50: WS2812B, LED_SMD:LED_WS2812B_PLCC4_5.0x5.0mm_P3.2mm, F.Cu at (155.1, 155.3)
- added RGB51: WS2812B, LED_SMD:LED_WS2812B_PLCC4_5.0x5.0mm_P3.2mm, F.Cu at (174.1, 155.3)
- added RGB52: WS2812B, LED_SMD:LED_WS2812B_PLCC4_5.0x5.0mm_P3.2mm, F.Cu at (193.1, 154.9)
- added RGB53: WS2812B, LED_SMD:LED_WS2812B_PLCC4_5.0x5.0mm_P3.2mm, F.Cu at (212.2, 154.1)
- added RGB54: WS2812B, LED_SMD:LED_WS2812B_PLCC4_5.0x5.0mm_P3.2mm, F.Cu at (231.3, 155.3)
- added RGB55: WS2812B, LED_SMD:LED_WS2812B_PLCC4_5.0x5.0mm_P3.2mm, F.Cu at (250.3, 155.3)
- added RGB56: WS2812B, LED_SMD:LED_WS2812B_PLCC4_5.0x5.0mm_P3.2mm, F.Cu at (274.2, 155.3)
- added RGB57: WS2812B, LED_SMD:LED_WS2812B_PLCC4_5.0x5.0mm_P3.2mm, F.Cu at (145.6, 174.4)
- added RGB58: WS2812B, LED_SMD:LED_WS2812B_PLCC4_5.0x5.0mm_P3.2mm, F.Cu at (164.6, 174.4)
- added RGB59: WS2812B, LED_SMD:LED_WS2812B_PLCC4_5.0x5.0mm_P3.2mm, F.Cu at (183.7, 174.4)
- added RGB6: WS2812B, LED_SMD:LED_WS2812B_PLCC4_5.0x5.0mm_P3.2mm, F.Cu at (88.4, 117.2)
- added RGB60: WS2812B, LED_SMD:LED_WS2812B_PLCC4_5.0x5.0mm_P3.2mm, F.Cu at (202.7, 174.4)
- added RGB61: WS2812B, LED_SMD:LED_WS2812B_PLCC4_5.0x5.0mm_P3.2mm, F.Cu at (221.8, 174.4)
- added RGB62: WS2812B, LED_SMD:LED_WS2812B_PLCC4_5.0x5.0mm_P3.2mm, F.Cu at (240.8, 174.4)
- added RGB63: WS2812B, LED_SMD:LED_WS2812B_PLCC4_5.0x5.0mm_P3.2mm, F.Cu at (269.4, 174.4)
- added RGB64: WS2812B, LED_SMD:LED_WS2812B_PLCC4_5.0x5.0mm_P3.2mm, F.Cu at (131.3, 193.4)
- added RGB65: WS2812B, LED_SMD:LED_WS2812B_PLCC4_5.0x5.0mm_P3.2mm, F.Cu at (150.3, 193.4)
- added RGB66: WS2812B, LED_SMD:LED_WS2812B_PLCC4_5.0x5.0mm_P3.2mm, F.Cu at (169.4, 193.4)
- added RGB67: WS2812B, LED_SMD:LED_WS2812B_PLCC4_5.0x5.0mm_P3.2mm, F.Cu at (188.4, 193.4)
- added RGB68: WS2812B, LED_SMD:LED_WS2812B_PLCC4_5.0x5.0mm_P3.2mm, F.Cu at (207.5, 193.4)
- added RGB69: WS2812B, LED_SMD:LED_WS2812B_PLCC4_5.0x5.0mm_P3.2mm, F.Cu at (226.5, 193.4)
- added RGB7: WS2812B, LED_SMD:LED_WS2812B_PLCC4_5.0x5.0mm_P3.2mm, F.Cu at (107.5, 117.2)
- added RGB70: WS2812B, LED_SMD:LED_WS2812B_PLCC4_5.0x5.0mm_P3.2mm, F.Cu at (262.3, 193.4)
- added RGB71: WS2812B, LED_SMD:LED_WS2812B_PLCC4_5.0x5.0mm_P3.2mm, F.Cu at (162.2, 212.5)
- added RGB72: WS2812B, LED_SMD:LED_WS2812B_PLCC4_5.0x5.0mm_P3.2mm, F.Cu at (205.1, 212.5)
- added RGB73: WS2812B, LED_SMD:LED_WS2812B_PLCC4_5.0x5.0mm_P3.2mm, F.Cu at (228.9, 212.5)
- added RGB74: WS2812B, LED_SMD:LED_WS2812B_PLCC4_5.0x5.0mm_P3.2mm, F.Cu at (252.7, 212.5)
- added RGB75: WS2812B, LED_SMD:LED_WS2812B_PLCC4_5.0x5.0mm_P3.2mm, F.Cu at (276.5, 212.5)
- added RGB76: WS2812B, LED_SMD:LED_WS2812B_PLCC4_5.0x5.0mm_P3.2mm, F.Cu at (317.0, 136.3)
- added RGB77: WS2812B, LED_SMD:LED_WS2812B_PLCC4_5.0x5.0mm_P3.2mm, F.Cu at (336.1, 136.3)
- added RGB78: WS2812B, LED_SMD:LED_WS2812B_PLCC4_5.0x5.0mm_P3.2mm, F.Cu at (355.1, 136.3)
- added RGB79: WS2812B, LED_SMD:LED_WS2812B_PLCC4_5.0x5.0mm_P3.2mm, F.Cu at (317.0, 155.3)
- added RGB8: WS2812B, LED_SMD:LED_WS2812B_PLCC4_5.0x5.0mm_P3.2mm, F.Cu at (-6.83, 136.3)
- added RGB80: WS2812B, LED_SMD:LED_WS2812B_PLCC4_5.0x5.0mm_P3.2mm, F.Cu at (336.1, 155.3)
- added RGB81: WS2812B, LED_SMD:LED_WS2812B_PLCC4_5.0x5.0mm_P3.2mm, F.Cu at (355.1, 155.3)
- added RGB82: WS2812B, LED_SMD:LED_WS2812B_PLCC4_5.0x5.0mm_P3.2mm, F.Cu at (317.0, 174.4)
- added RGB83: WS2812B, LED_SMD:LED_WS2812B_PLCC4_5.0x5.0mm_P3.2mm, F.Cu at (336.1, 174.4)
- added RGB84: WS2812B, LED_SMD:LED_WS2812B_PLCC4_5.0x5.0mm_P3.2mm, F.Cu at (355.1, 174.4)
- added RGB85: WS2812B, LED_SMD:LED_WS2812B_PLCC4_5.0x5.0mm_P3.2mm, F.Cu at (336.1, 193.4)
- added RGB86: WS2812B, LED_SMD:LED_WS2812B_PLCC4_5.0x5.0mm_P3.2mm, F.Cu at (317.0, 212.5)
- added RGB87: WS2812B, LED_SMD:LED_WS2812B_PLCC4_5.0x5.0mm_P3.2mm, F.Cu at (336.1, 212.5)
- added RGB88: WS2812B, LED_SMD:LED_WS2812B_PLCC4_5.0x5.0mm_P3.2mm, F.Cu at (355.1, 212.5)
- added RGB89: WS2812B, LED_SMD:LED_WS2812B_PLCC4_5.0x5.0mm_P3.2mm, F.Cu at (393.2, 136.3)
- added RGB9: WS2812B, LED_SMD:LED_WS2812B_PLCC4_5.0x5.0mm_P3.2mm, F.Cu at (12.2, 136.3)
- added RGB90: WS2812B, LED_SMD:LED_WS2812B_PLCC4_5.0x5.0mm_P3.2mm, F.Cu at (412.3, 136.3)
- added RGB91: WS2812B, LED_SMD:LED_WS2812B_PLCC4_5.0x5.0mm_P3.2mm, F.Cu at (431.3, 136.3)
- added RGB92: WS2812B, LED_SMD:LED_WS2812B_PLCC4_5.0x5.0mm_P3.2mm, F.Cu at (450.4, 136.3)
- added RGB93: WS2812B, LED_SMD:LED_WS2812B_PLCC4_5.0x5.0mm_P3.2mm, F.Cu at (393.2, 155.3)
- added RGB94: WS2812B, LED_SMD:LED_WS2812B_PLCC4_5.0x5.0mm_P3.2mm, F.Cu at (412.3, 155.3)
- added RGB95: WS2812B, LED_SMD:LED_WS2812B_PLCC4_5.0x5.0mm_P3.2mm, F.Cu at (431.3, 155.3)
- added RGB96: WS2812B, LED_SMD:LED_WS2812B_PLCC4_5.0x5.0mm_P3.2mm, F.Cu at (450.4, 155.3)
- added RGB97: WS2812B, LED_SMD:LED_WS2812B_PLCC4_5.0x5.0mm_P3.2mm, F.Cu at (393.2, 174.4)
- added RGB98: WS2812B, LED_SMD:LED_WS2812B_PLCC4_5.0x5.0mm_P3.2mm, F.Cu at (412.3, 174.4)
- added RGB99: WS2812B, LED_SMD:LED_WS2812B_PLCC4_5.0x5.0mm_P3.2mm, F.Cu at (431.3, 174.4)
- added SR10: 74HC165, Arduino_Pro_Micro:R-PDSO-G16, F.Cu at (164.7, 39.6)
- added SR11: 74HC165, Arduino_Pro_Micro:R-PDSO-G16, F.Cu at (268.7, 37.0)
- added SR12: 74HC165, Arduino_Pro_Micro:R-PDSO-G16, F.Cu at (267.8, 9.98)
- added SR13: 74HC165, Arduino_Pro_Micro:R-PDSO-G16, F.Cu at (187.9, 38.3)
- added SR14: 74HC165, Arduino_Pro_Micro:R-PDSO-G16, F.Cu at (199.4, 38.3)
- added SR15: 74HC165, Arduino_Pro_Micro:R-PDSO-G16, F.Cu at (210.9, 38.3)
- added SR16: 74HC165, Arduino_Pro_Micro:R-PDSO-G16, F.Cu at (222.5, 38.3)
- added SR17: 74HC165, Arduino_Pro_Micro:R-PDSO-G16, F.Cu at (234.0, 38.3)
- added SR18: 74HC165, Arduino_Pro_Micro:R-PDSO-G16, F.Cu at (245.5, 38.3)
- added SR19: 74HC165, Arduino_Pro_Micro:R-PDSO-G16, F.Cu at (257.0, 37.6)
- added SR20: 74HC165, Arduino_Pro_Micro:R-PDSO-G16, F.Cu at (292.9, 0.00)
- added SR21: 74HC165, Arduino_Pro_Micro:R-PDSO-G16, F.Cu at (289.1, 19.1)
- added SR22: 74HC165, Arduino_Pro_Micro:R-PDSO-G16, F.Cu at (176.2, 39.6)
- added SR4: 74HC165, Arduino_Pro_Micro:R-PDSO-G16, F.Cu at (267.8, 19.0)
- added SR5: 74HC165, Arduino_Pro_Micro:R-PDSO-G16, F.Cu at (107.1, 39.6)
- added SR6: 74HC165, Arduino_Pro_Micro:R-PDSO-G16, F.Cu at (118.6, 39.6)
- added SR7: 74HC165, Arduino_Pro_Micro:R-PDSO-G16, F.Cu at (130.1, 39.6)
- added SR8: 74HC165, Arduino_Pro_Micro:R-PDSO-G16, F.Cu at (141.7, 39.6)
- added SR9: 74HC165, Arduino_Pro_Micro:R-PDSO-G16, F.Cu at (153.2, 39.6)
- added SW10: F5, Button_Switch_Keyboard:SW_Cherry_MX_1.00u_PCB, F.Cu at (85.9, 128.3)
- added SW100: LSPACE, Cherry_MX_SMD:SW_Cherry_MX_3.00u_PCB, F.Cu at (83.7, 218.5)
- added SW101: RSPACE, Cherry_MX_SMD:SW_Cherry_MX_3.25u_PCB, F.Cu at (162.2, 218.5)
- added SW102: ALTGR, Button_Switch_Keyboard:SW_Cherry_MX_1.25u_PCB, F.Cu at (202.6, 223.5)
- added SW103: FN, Button_Switch_Keyboard:SW_Cherry_MX_1.25u_PCB, F.Cu at (226.4, 223.5)
- added SW104: MENU, Button_Switch_Keyboard:SW_Cherry_MX_1.25u_PCB, F.Cu at (250.2, 223.5)
- added SW105: RCTRL, Button_Switch_Keyboard:SW_Cherry_MX_1.25u_PCB, F.Cu at (274.0, 223.5)
- added SW106: LEFT, Button_Switch_Keyboard:SW_Cherry_MX_1.00u_PCB, F.Cu at (314.5, 223.5)
- added SW107: DOWN, Button_Switch_Keyboard:SW_Cherry_MX_1.00u_PCB, F.Cu at (333.5, 223.5)
- added SW108: RIGHT, Button_Switch_Keyboard:SW_Cherry_MX_1.00u_PCB, F.Cu at (352.6, 223.5)
- added SW109: MACRO17, Button_Switch_Keyboard:SW_Cherry_MX_1.00u_PCB, F.Cu at (390.7, 223.5)
- added SW11: F6, Button_Switch_Keyboard:SW_Cherry_MX_1.00u_PCB, F.Cu at (104.9, 128.3)
- added SW110: MACRO18, Button_Switch_Keyboard:SW_Cherry_MX_1.00u_PCB, F.Cu at (409.7, 223.5)
- added SW111: MACRO19, Button_Switch_Keyboard:SW_Cherry_MX_1.00u_PCB, F.Cu at (428.8, 223.5)
- added SW112: MACRO20, Button_Switch_Keyboard:SW_Cherry_MX_1.00u_PCB, F.Cu at (447.8, 223.5)
- added SW12: F7, Button_Switch_Keyboard:SW_Cherry_MX_1.00u_PCB, F.Cu at (143.0, 128.3)
- added SW13: F8, Button_Switch_Keyboard:SW_Cherry_MX_1.00u_PCB, F.Cu at (162.1, 128.3)
- added SW14: F9, Button_Switch_Keyboard:SW_Cherry_MX_1.00u_PCB, F.Cu at (181.1, 128.3)
- added SW15: F10, Button_Switch_Keyboard:SW_Cherry_MX_1.00u_PCB, F.Cu at (200.2, 128.3)
- added SW16: F11, Button_Switch_Keyboard:SW_Cherry_MX_1.00u_PCB, F.Cu at (219.2, 128.3)
- added SW17: F12, Button_Switch_Keyboard:SW_Cherry_MX_1.00u_PCB, F.Cu at (238.3, 128.3)
- added SW18: PRTSCR, Button_Switch_Keyboard:SW_Cherry_MX_1.00u_PCB, F.Cu at (314.5, 147.3)
- added SW19: SCRLOCK, Button_Switch_Keyboard:SW_Cherry_MX_1.00u_PCB, F.Cu at (333.5, 147.3)
- added SW20: PAUSE, Button_Switch_Keyboard:SW_Cherry_MX_1.00u_PCB, F.Cu at (352.6, 147.3)
- added SW21: `, Button_Switch_Keyboard:SW_Cherry_MX_1.00u_PCB, F.Cu at (-9.37, 147.3)
- added SW22: 1, Button_Switch_Keyboard:SW_Cherry_MX_1.00u_PCB, F.Cu at (9.68, 147.3)
- added SW23: 2, Button_Switch_Keyboard:SW_Cherry_MX_1.00u_PCB, F.Cu at (28.7, 147.3)
- added SW24: 3, Button_Switch_Keyboard:SW_Cherry_MX_1.00u_PCB, F.Cu at (47.8, 147.3)
- added SW25: 4, Button_Switch_Keyboard:SW_Cherry_MX_1.00u_PCB, F.Cu at (66.8, 147.3)
- added SW26: 5, Button_Switch_Keyboard:SW_Cherry_MX_1.00u_PCB, F.Cu at (85.9, 147.3)
- added SW27: 6, Button_Switch_Keyboard:SW_Cherry_MX_1.00u_PCB, F.Cu at (104.9, 147.3)
- added SW28: 7, Button_Switch_Keyboard:SW_Cherry_MX_1.00u_PCB, F.Cu at (143.0, 147.3)
- added SW29: 8, Button_Switch_Keyboard:SW_Cherry_MX_1.00u_PCB, F.Cu at (162.1, 147.3)
- added SW30: 9, Button_Switch_Keyboard:SW_Cherry_MX_1.00u_PCB, F.Cu at (181.1, 147.3)
- added SW31: 0, Button_Switch_Keyboard:SW_Cherry_MX_1.00u_PCB, F.Cu at (200.2, 147.3)
- added SW32: -, Button_Switch_Keyboard:SW_Cherry_MX_1.00u_PCB, F.Cu at (219.2, 147.3)
- added SW33: =, Button_Switch_Keyboard:SW_Cherry_MX_1.00u_PCB, F.Cu at (238.3, 147.3)
- added SW34: BACKSPACE, Button_Switch_Keyboard:SW_Cherry_MX_2.00u_PCB, F.Cu at (266.9, 147.3)
- added SW35: INSERT, Button_Switch_Keyboard:SW_Cherry_MX_1.00u_PCB, F.Cu at (314.5, 166.4)
- added SW36: HOME, Button_Switch_Keyboard:SW_Cherry_MX_1.00u_PCB, F.Cu at (333.5, 166.4)
- added SW37: PGUP, Button_Switch_Keyboard:SW_Cherry_MX_1.00u_PCB, F.Cu at (352.6, 166.4)
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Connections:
- R15 pad 1: +5V -> SW4
- R16 pad 1: +5V -> A5
- R16 pad 2: Net-(C2-Pad2) -> +5V
- R17 pad 2: Net-(C3-Pad2) -> B5
- R18 pad 1: +5V -> SW3
- R19 pad 1: Net-(R19-Pad1) -> A6
- R19 pad 2: Net-(MX1-Pad6) -> +5V
- R20 pad 1: Net-(R20-Pad1) -> +5V
- R20 pad 2: Net-(MX2-Pad6) -> B6
- R21 pad 1: Net-(R21-Pad1) -> SW2
- R22 pad 1: Net-(R22-Pad1) -> A7
- R22 pad 2: Net-(MX4-Pad6) -> +5V
- R23 pad 1: Net-(R23-Pad1) -> +5V
- R23 pad 2: RGB -> B7
- SR1 pad 3: Net-(R19-Pad1) -> Net-(SR1-Pad3)
- SR1 pad 4: Net-(R20-Pad1) -> Net-(SR1-Pad4)
- SR1 pad 5: Net-(R21-Pad1) -> Net-(SR1-Pad5)
- SR1 pad 6: Net-(R22-Pad1) -> Net-(SR1-Pad6)
- SR3 pad 11: SW1 -> Net-(SR3-Pad11)
- SR3 pad 12: SW2 -> Net-(SR3-Pad12)
- SR3 pad 13: SW3 -> Net-(SR3-Pad13)
- SR3 pad 14: SW4 -> Net-(SR3-Pad14)
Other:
- board outline removed
- board text removed: "D+"
- board text removed: "D-"
- board text removed: "GND"
- board text removed: "RGB"
- board text removed: "VCC"
